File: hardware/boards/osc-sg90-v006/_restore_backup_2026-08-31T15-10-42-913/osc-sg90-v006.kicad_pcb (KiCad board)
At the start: 4 copper layers, 12.1 x 9.6 mm, 34 parts, among them J1 Servo Input, J2 Motor, J3 Debug, J4 Potentiometer, U1 H7133-1_C277537, U4 DRV8837, U5 CH32V006F8U6, U6 74LVC2G241GS,115, U7 ECC204-MAVCZ-T

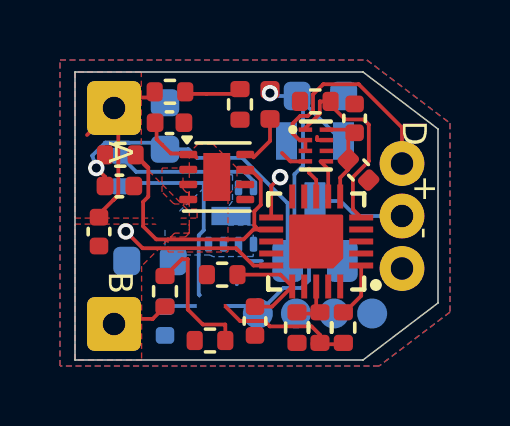
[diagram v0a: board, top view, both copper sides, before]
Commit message: fixing drc and routing
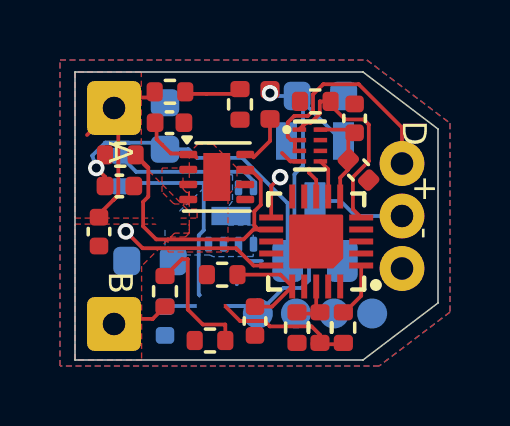
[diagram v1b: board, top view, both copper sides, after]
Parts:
- moved U6 0.20 mm to (107.8, 92.7)
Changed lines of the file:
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@@
 	(footprint "shared:XSON-8_L1.4-W1.0-P0.35-S0.55-BL"
 		(layer "F.Cu")
-		(at 108.03 92.65 -90)
+		(at 107.83 92.65 -90)
 		(property "Reference" "U6"
 			(at 0 -4.35 90)
@@
 	)
 	(segment
+		(start 108.03 92.12)
+		(end 109.215 92.12)
+		(width 0.127)
+		(layer "F.Cu")
+		(net "+3V3")
+	)
+	(segment
 		(start 108.165 99.23)
 		(end 108.165 98.960001)
@@
 	)
 	(segment
-		(start 109.215 92.12)
-		(end 109.32 92.225)
-		(width 0.2)
-		(layer "F.Cu")
-		(net "+3V3")
-	)
-	(segment
 		(start 109.1106 92.4344)
 		(end 109.32 92.225)
@@
 	)
 	(segment
-		(start 107.884999 98.68)
-		(end 106.494714 98.68)
-		(width 0.127)
+		(start 109.215 92.12)
+		(end 109.32 92.225)
+		(width 0.2)
 		(layer "F.Cu")
 		(net "+3V3")
 	)
 	(segment
-		(start 108.84 94.35)
-		(end 108.84 93.7213)
+		(start 107.884999 98.68)
+		(end 106.494714 98.68)
 		(width 0.127)
 		(layer "F.Cu")
@@
 	)
 	(segment
-		(start 108.38 92.12)
-		(end 109.215 92.12)
+		(start 108.84 94.35)
+		(end 108.84 93.7213)
 		(width 0.127)
 		(layer "F.Cu")
@@
 	)
 	(segment
-		(start 107.5 91.2)
-		(end 107.5 91.18)
-		(width 0.127)
-		(layer "F.Cu")
-		(net "GND")
-	)
-	(segment
-		(start 107.5 91.2)
-		(end 107.6 91.3)
-		(width 0.127)
-		(layer "F.Cu")
-		(net "GND")
-	)
-	(segment
 		(start 107.18 93.18)
 		(end 106.9 92.9)
@@
 	)
 	(segment
-		(start 108.1605 91.18)
-		(end 108.160499 91.586411)
+		(start 108.160499 91.586411)
+		(end 107.85641 91.8905)
 		(width 0.127)
 		(layer "F.Cu")
@@
 	)
 	(segment
-		(start 108.160499 91.586411)
-		(end 107.68 92.06691)
+		(start 108.52 91.18)
+		(end 108.1605 91.18)
 		(width 0.127)
 		(layer "F.Cu")
@@
 	)
 	(segment
-		(start 108.0685 92.45541)
-		(end 108.0685 92.3585)
-		(width 0.127)
-		(layer "F.Cu")
-		(net "/TX_EN")
-	)
-	(segment
 		(start 109.7935 93.173118)
 		(end 109.7935 91.955406)
@@
 	)
 	(segment
-		(start 108.08309 92.47)
-		(end 108.0685 92.45541)
+		(start 107.85641 91.8905)
+		(end 107.7095 91.8905)
 		(width 0.127)
 		(layer "F.Cu")
@@
 	)
 	(segment
-		(start 108.38 92.47)
-		(end 108.08309 92.47)
+		(start 107.7095 91.8905)
+		(end 107.6 92)
 		(width 0.127)
 		(layer "F.Cu")
@@
 	)
 	(segment
-		(start 108.52 91.18)
-		(end 108.1605 91.18)
+		(start 109.7935 91.955406)
+		(end 109.619594 91.7815)
 		(width 0.127)
 		(layer "F.Cu")
@@
 	)
 	(segment
-		(start 109.7935 91.955406)
-		(end 109.619594 91.7815)
+		(start 107.6 92)
+		(end 107.5 92.1)
 		(width 0.127)
 		(layer "F.Cu")
@@
 	)
 	(segment
-		(start 107.68 92.06691)
-		(end 107.68 92.12)
+		(start 108.1605 91.18)
+		(end 108.160499 91.586411)
 		(width 0.127)
 		(layer "F.Cu")
@@
 	)
 	(segment
+		(start 107.6 92)
+		(end 107.48 92.12)
+		(width 0.127)
+		(layer "F.Cu")
+		(net "/TX_EN")
+	)
+	(segment
 		(start 108.44 93.44)
 		(end 108.18 93.18)
@@
 	)
 	(segment
-		(start 107.509499 91.663501)
-		(end 107.253001 91.919999)
+		(start 109.4561 90.6073)
+		(end 108.2757 90.6073)
 		(width 0.127)
 		(layer "F.Cu")
@@
 	)
 	(segment
-		(start 107.9335 90.9495)
-		(end 107.9335 91.492384)
+		(start 110.9 92.0512)
+		(end 109.4561 90.6073)
 		(width 0.127)
 		(layer "F.Cu")
@@
 	)
 	(segment
-		(start 108.2757 90.6073)
-		(end 107.9335 90.9495)
+		(start 110.9 93.25)
+		(end 110.9 92.0512)
 		(width 0.127)
 		(layer "F.Cu")
@@
 	)
 	(segment
-		(start 107.253001 91.919999)
-		(end 107.253001 92.243001)
+		(start 107.0915 92.3585)
+		(end 107.203 92.47)
 		(width 0.127)
 		(layer "F.Cu")
@@
 	(segment
 		(start 107.762384 91.6635)
-		(end 107.509499 91.663501)
+		(end 107.3095 91.6635)
 		(width 0.127)
 		(layer "F.Cu")
@@
 	)
 	(segment
-		(start 107.9335 91.492384)
-		(end 107.762384 91.6635)
+		(start 107.3095 91.6635)
+		(end 107.0915 91.8815)
 		(width 0.127)
 		(layer "F.Cu")
@@
 	)
 	(segment
-		(start 107.68 92.47)
-		(end 107.68 92.83)
+		(start 107.203 92.47)
+		(end 107.48 92.47)
 		(width 0.127)
 		(layer "F.Cu")
@@
 	)
 	(segment
-		(start 109.4561 90.6073)
-		(end 108.2757 90.6073)
+		(start 107.33 92.47)
+		(end 107.33 92.83)
 		(width 0.127)
 		(layer "F.Cu")
@@
 	)
 	(segment
-		(start 110.9 92.0512)
-		(end 109.4561 90.6073)
+		(start 108.2757 90.6073)
+		(end 107.9335 90.9495)
 		(width 0.127)
 		(layer "F.Cu")
@@
 	)
 	(segment
-		(start 110.9 93.25)
-		(end 110.9 92.0512)
+		(start 107.0915 91.8815)
+		(end 107.0915 92.3585)
 		(width 0.127)
 		(layer "F.Cu")
@@
 	)
 	(segment
-		(start 107.253001 92.243001)
-		(end 107.48 92.47)
+		(start 107.9335 91.492384)
+		(end 107.762384 91.6635)
+		(width 0.127)
+		(layer "F.Cu")
+		(net "/DATA")
+	)
+	(segment
+		(start 107.9335 90.9495)
+		(end 107.9335 91.492384)
 		(width 0.127)
 		(layer "F.Cu")
